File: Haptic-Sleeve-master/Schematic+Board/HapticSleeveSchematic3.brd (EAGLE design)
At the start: 100 x 80 mm, 15 parts, among them IC1 A3946KLP-T, IC2 A3946KLP-T, M1 MOTOR10MM, M2 MOTOR10MM, M3 MOTOR10MM, M4 MOTOR10MM

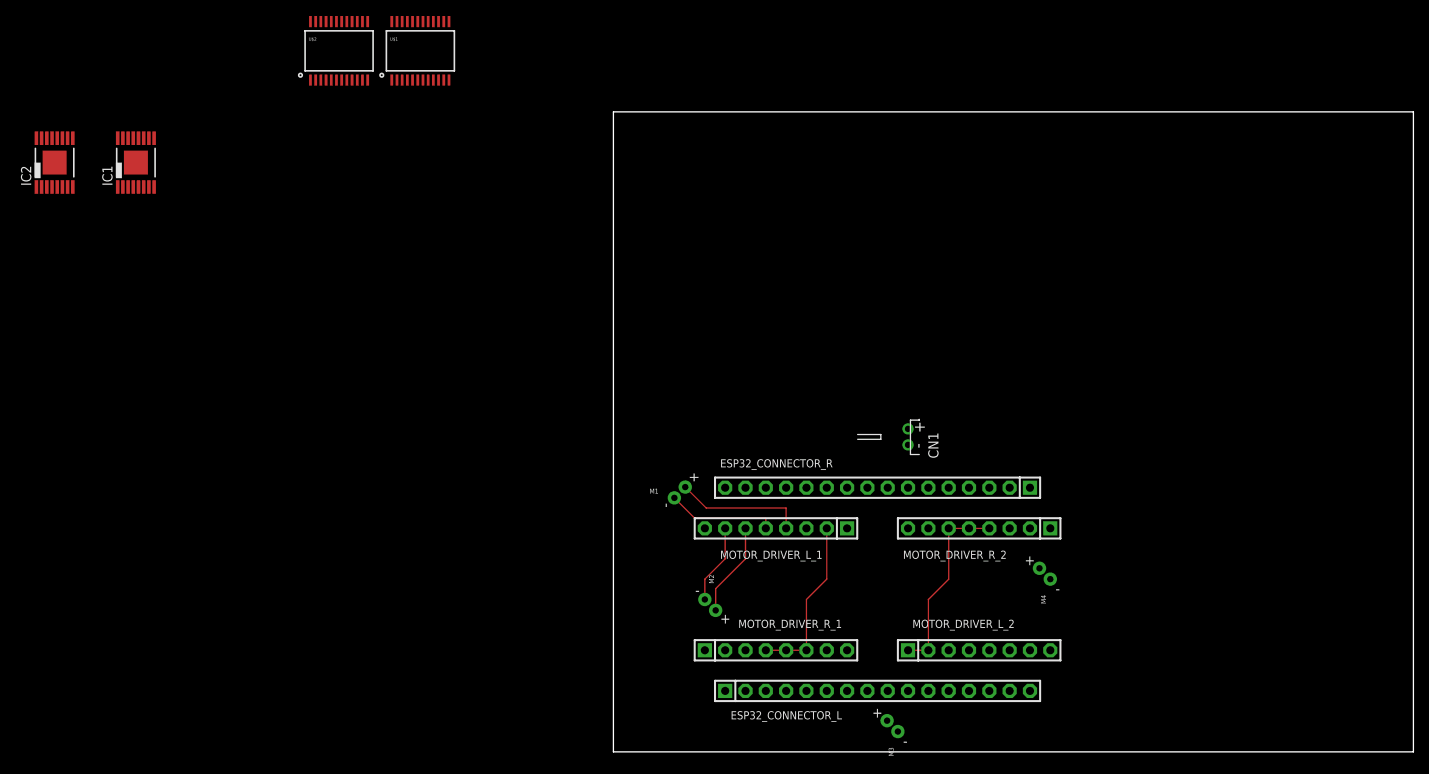
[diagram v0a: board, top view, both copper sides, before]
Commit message: HapticSleeveSchematic3.brd has 4 motors on one side of board with more routing. HapticSleeveSchematic3 - Copy.brd has 2 motors on each side of the board with less routing
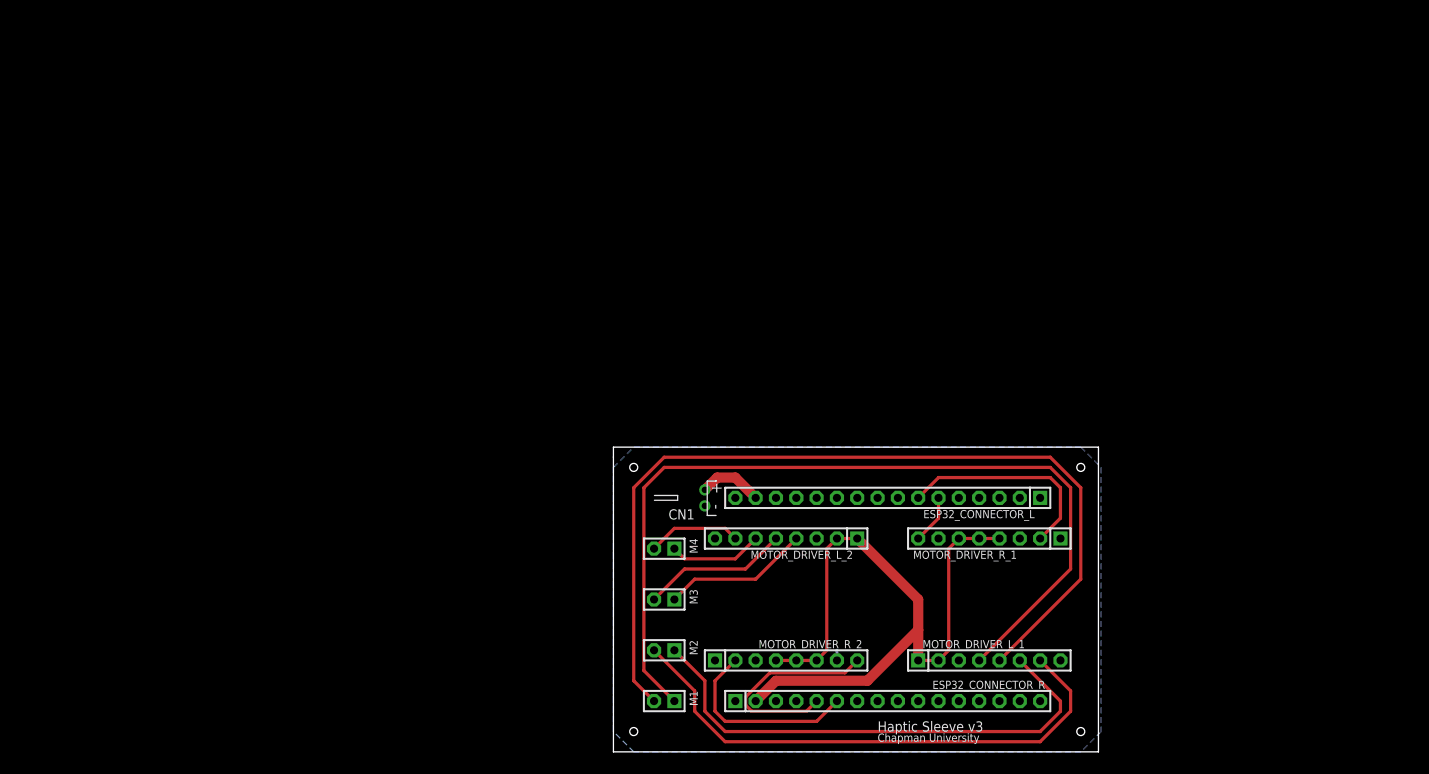
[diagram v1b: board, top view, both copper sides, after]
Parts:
- removed IC1, IC2: A3946KLP-T, allegro:TSSOP16E
- removed U$1, U$2: TB6612FNG, SparkFun-IC-Special-Function:SSOP24
- M1, M2, M3, M4: value MOTOR10MM -> F-1X02-SIP-100-40; device SparkFun-Electromechanical:VIBE-MOTOR-10MM -> con-headers-jp-1:SIP-100-02-40
- moved M4 42.4 mm to (6.35, 25.4)
- moved M1 31.8 mm to (6.35, 6.35), turned to 180 degrees
- moved MOTOR_DRIVER_L_1 31.4 mm to (47.0, 11.4), turned to 0 degrees
- moved MOTOR_DRIVER_R_1 30.1 mm to (47.0, 26.7), turned to 180 degrees
- moved M3 29.8 mm to (6.35, 19.1)
- moved MOTOR_DRIVER_R_2 29.2 mm to (21.6, 11.4), turned to 0 degrees
- moved MOTOR_DRIVER_L_2 27.9 mm to (21.6, 26.7), turned to 180 degrees
- moved ESP32_CONNECTOR_R 26.7 mm to (34.3, 6.35), turned to 0 degrees
- moved CN1 26.5 mm to (11.4, 31.8)
- moved ESP32_CONNECTOR_L 24.2 mm to (34.3, 31.8), turned to 180 degrees
- moved M2 14.5 mm to (6.35, 12.7), turned to 180 degrees
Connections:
- removed net LGND: IC1.13, IC2.13
- removed net PGND: IC1.4, IC2.4
- net M1+: now also M1.1; no longer M1.+
- net M1-: now also M1.2; no longer M1.-
- net M2+: now also M2.1; no longer M2.+
- net M2-: now also M2.2; no longer M2.-
- net M3+: now also M3.1; no longer M3.+
- net M3-: now also M3.2; no longer M3.-
- net M4+: now also M4.1; no longer M4.+
- net M4-: now also M4.2; no longer M4.-
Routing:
- net M1-: track 13.8 -> 112.8 mm
- net M1+: track 16.2 -> 110.2 mm
- net M2-: track 9.94 -> 67.8 mm
- net M2+: track 11.8 -> 64.2 mm
- net 3V3: track 45.3 -> 90.2 mm
- net MOTOR2: track 0.00 -> 26.8 mm
- net MOTOR3: track 0.00 -> 26.6 mm
- net MOTOR4: track 0.00 -> 24.2 mm
- net M3-: track 0.00 -> 18.4 mm
- net M3+: track 0.00 -> 18.4 mm
- net M4-: track 0.00 -> 11.7 mm
- net M4+: track 0.00 -> 11.7 mm
- net VCC: track 0.00 -> 8.04 mm
- net MOTOR1: track 0.00 -> 6.13 mm
- net GND: track 0.00 -> 1.27 mm
- added copper zone on layer 16, net GND
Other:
- board size 100 x 80 mm -> 60.6 x 38.1 mm
- board text added: "Chapman University"
- board text added: "Haptic Sleeve v3"
